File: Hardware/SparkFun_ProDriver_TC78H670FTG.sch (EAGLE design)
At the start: 50 parts, among them J1 POWER_JACKTOE, J2 LATCH, J3 PTH, J4 LATCH, J5 LATCH, J6 PTH, J7 LATCH, J8 PTH, U1 TC78H670FTG, U2 LM1117

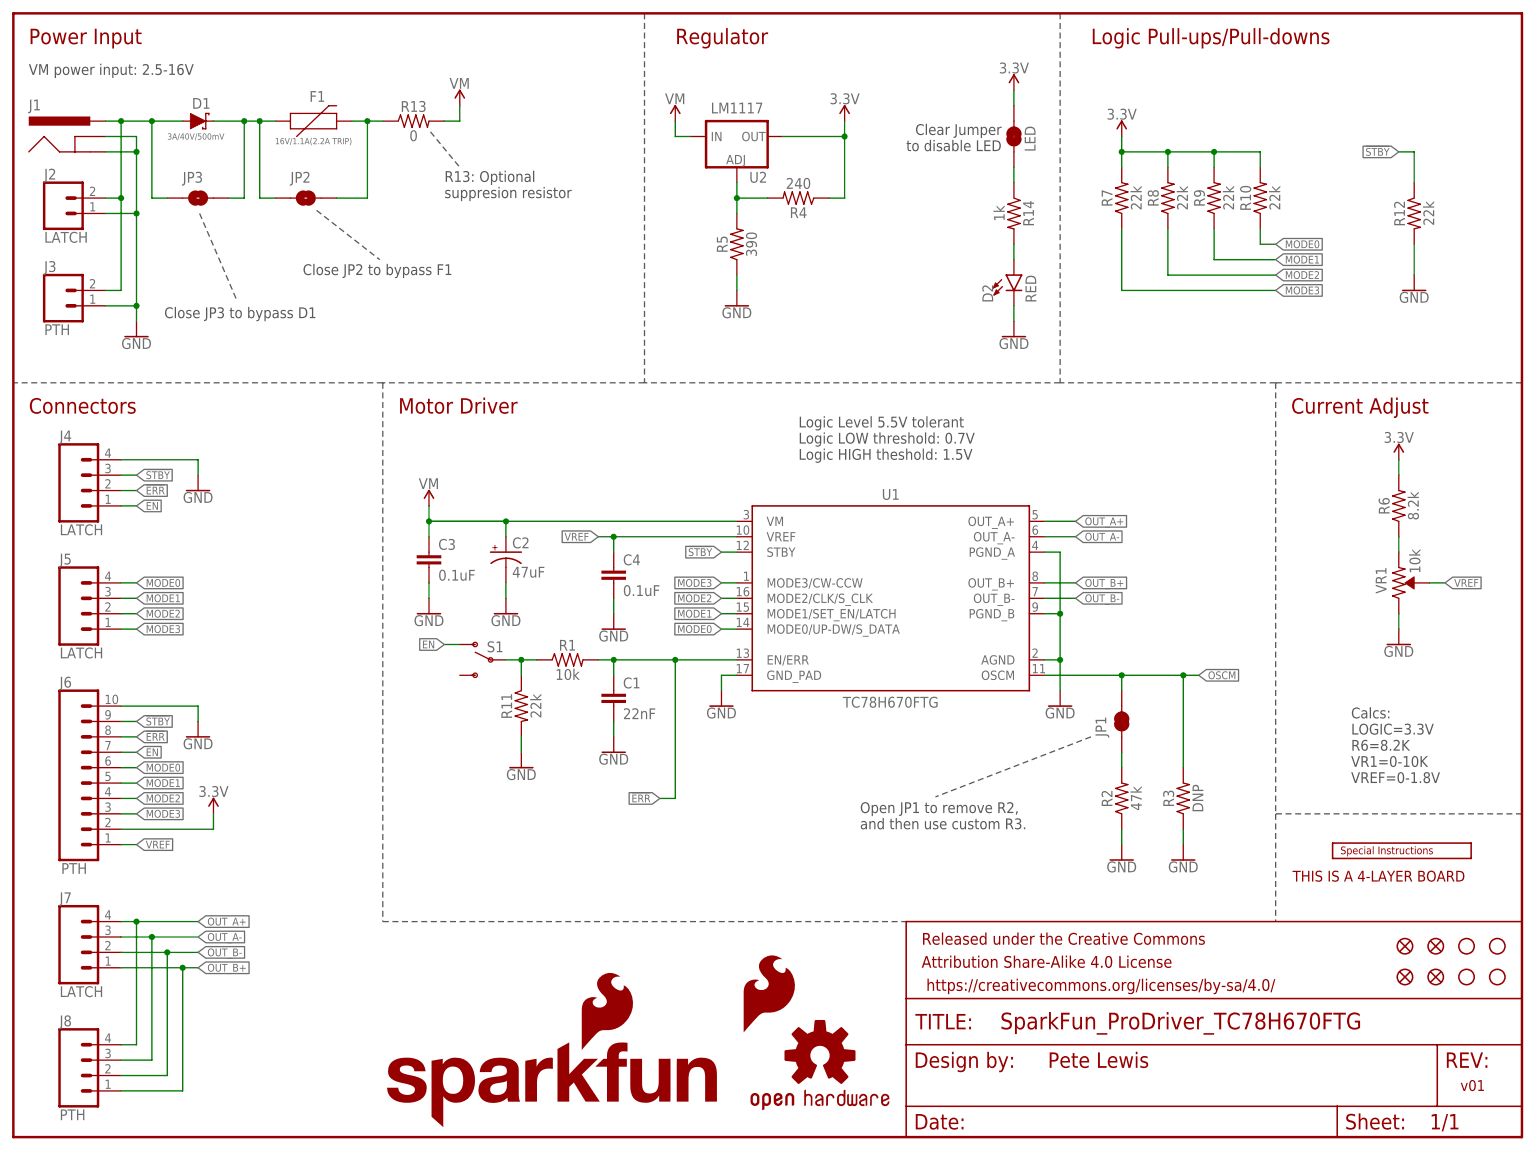
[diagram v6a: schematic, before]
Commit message: Suggestions from design review
-Jumper names same in sch and brd labels
-JP1 to OSCM
-ERR net position aligned with others
-changed power input silk to 3.3V-16V, also updated sch
-added more vias near IC, head sink exposed copper, and VM input traces to help heat transfer to inner layers.
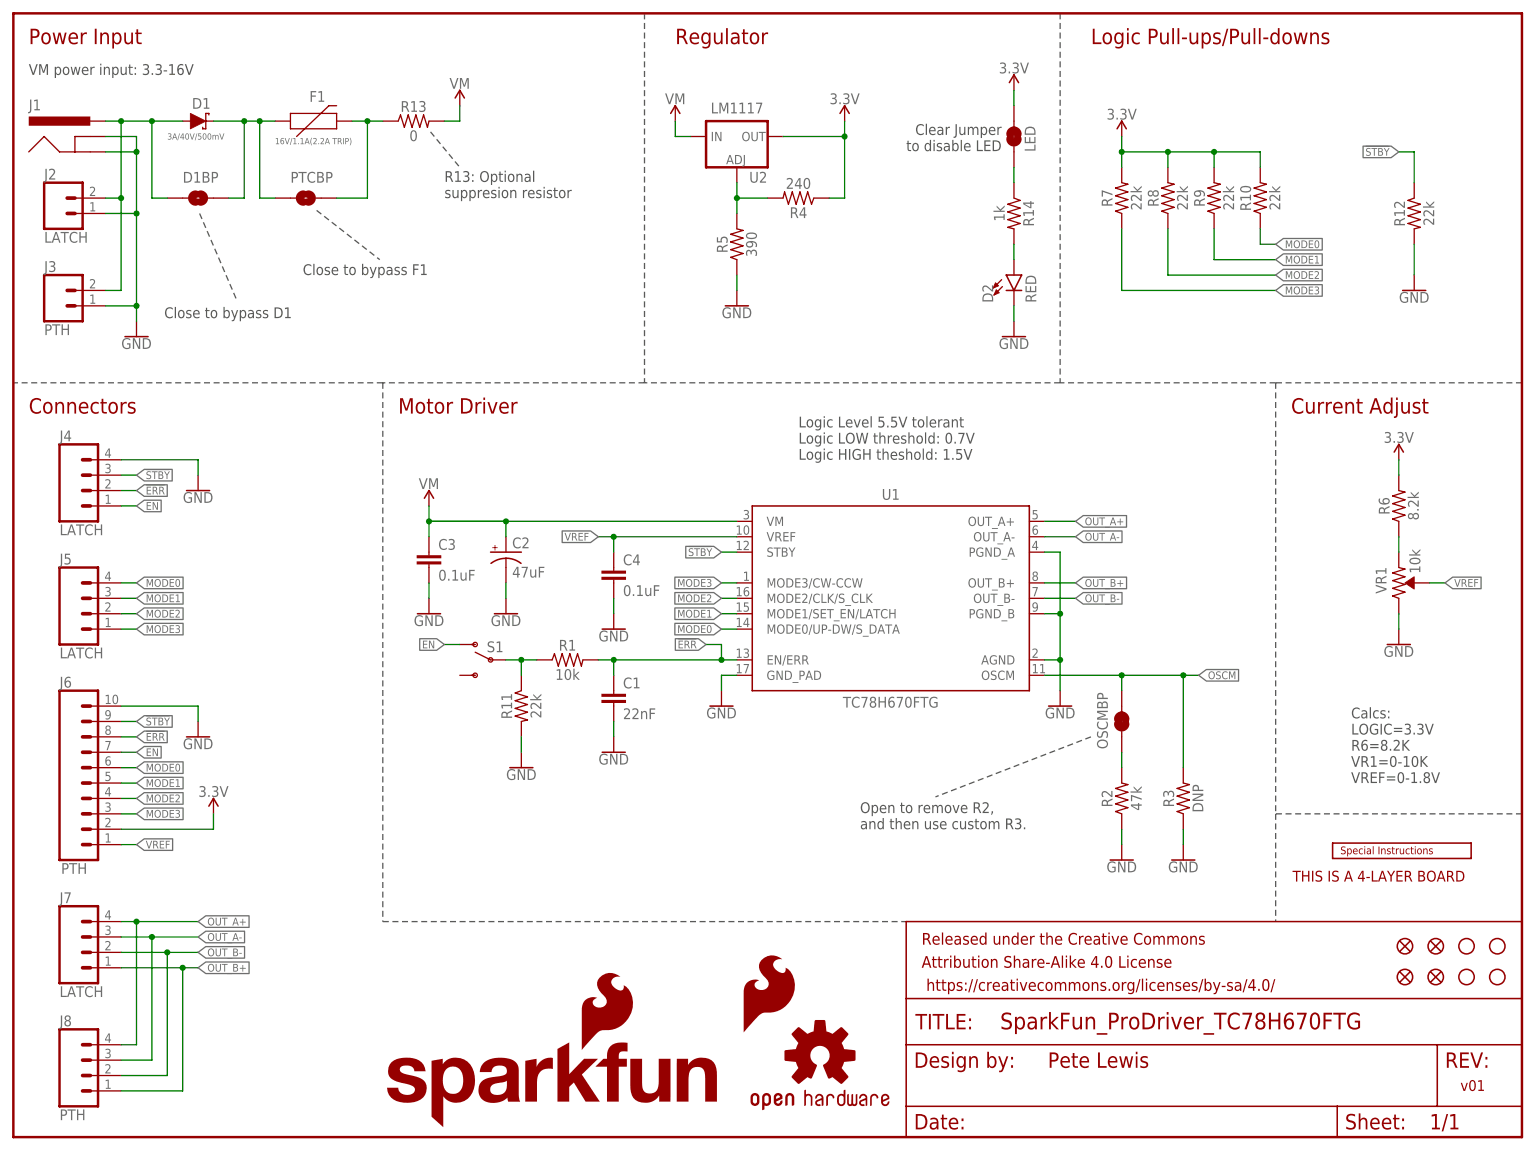
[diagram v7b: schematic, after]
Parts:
- renumbered JP1 to OSCMBP, JP2 to PTCBP, JP3 to D1BP
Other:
- note added: "Close to bypass D1"
- note added: "Close to bypass F1"
- note added: "Open to remove R2, and then use custom R3."
- note added: "VM power input: 3.3-16V"
- note removed: "Close JP2 to bypass F1"
- note removed: "Close JP3 to bypass D1"
- note removed: "Open JP1 to remove R2, and then use custom R3."
- note removed: "VM power input: 2.5-16V"
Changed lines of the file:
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@@
 <part name="R3" library="SparkFun-Resistors" deviceset="RESISTOR" device="AXIAL-0.3" value="DNP"/>
 <part name="GND5" library="SparkFun-PowerSymbols" deviceset="GND" device=""/>
-<part name="JP1" library="SparkFun-Jumpers" deviceset="JUMPER-SMT_2_NC_TRACE" device="_SILK" package3d_urn="urn:adsk.eagle:package:39281/1" value=""/>
+<part name="OSCMBP" library="SparkFun-Jumpers" deviceset="JUMPER-SMT_2_NC_TRACE" device="_SILK" package3d_urn="urn:adsk.eagle:package:39281/1" value=""/>
 <part name="GND6" library="SparkFun-PowerSymbols" deviceset="GND" device=""/>
 <part name="SUPPLY2" library="SparkFun-PowerSymbols" deviceset="VCC" device="" value="VM"/>
@@
 <part name="F1" library="TC78H670FTG" deviceset="PPTC" device="_16V_1.1A_(2.2ATRIP)" value="16V/1.1A(2.2A TRIP)"/>
 <part name="R13" library="SparkFun-Resistors" library_urn="urn:adsk.eagle:library:532" deviceset="0OHM" device="-0603-1/10W-5%" package3d_urn="urn:adsk.eagle:package:39650/1" value="0"/>
-<part name="JP2" library="SparkFun-Jumpers" library_urn="urn:adsk.eagle:library:528" deviceset="JUMPER-SMT_2_NO" device="_SILK" package3d_urn="urn:adsk.eagle:package:39279/1" value=""/>
-<part name="JP3" library="SparkFun-Jumpers" library_urn="urn:adsk.eagle:library:528" deviceset="JUMPER-SMT_2_NO" device="_SILK" package3d_urn="urn:adsk.eagle:package:39279/1" value=""/>
+<part name="PTCBP" library="SparkFun-Jumpers" library_urn="urn:adsk.eagle:library:528" deviceset="JUMPER-SMT_2_NO" device="_SILK" package3d_urn="urn:adsk.eagle:package:39279/1" value=""/>
+<part name="D1BP" library="SparkFun-Jumpers" library_urn="urn:adsk.eagle:library:528" deviceset="JUMPER-SMT_2_NO" device="_SILK" package3d_urn="urn:adsk.eagle:package:39279/1" value=""/>
 <part name="D2" library="SparkFun-LED" deviceset="LED-RED" device="0603" value="RED"/>
 <part name="R14" library="SparkFun-Resistors" deviceset="1KOHM" device="-0603-1/10W-1%" value="1k"/>
@@
 <wire x1="208.28" y1="53.34" x2="208.28" y2="35.56" width="0.2032" layer="97" style="longdash"/>
 <wire x1="104.14" y1="185.42" x2="104.14" y2="124.46" width="0.2032" layer="97" style="longdash"/>
-<text x="139.7" y="50.8" size="1.778" layer="97" font="vector">Open JP1 to remove R2,
+<text x="139.7" y="50.8" size="1.778" layer="97" font="vector">Open to remove R2,
 and then use custom R3.</text>
 <wire x1="177.8" y1="66.04" x2="152.146" y2="56.134" width="0.1524" layer="97" style="shortdash"/>
-<text x="47.752" y="142.24" size="1.778" layer="97" font="vector">Close JP2 to bypass F1</text>
-<text x="24.892" y="135.128" size="1.778" layer="97" font="vector">Close JP3 to bypass D1</text>
+<text x="47.752" y="142.24" size="1.778" layer="97" font="vector">Close to bypass F1</text>
+<text x="24.892" y="135.128" size="1.778" layer="97" font="vector">Close to bypass D1</text>
 <wire x1="30.734" y1="152.4" x2="36.83" y2="138.176" width="0.1524" layer="97" style="shortdash"/>
 <wire x1="50.038" y1="152.908" x2="60.452" y2="144.78" width="0.1524" layer="97" style="shortdash"/>
@@
 to disable LED</text>
 <wire x1="172.72" y1="185.42" x2="172.72" y2="124.46" width="0.2032" layer="97" style="longdash"/>
-<text x="2.54" y="175.26" size="1.778" layer="97" font="vector">VM power input: 2.5-16V</text>
+<text x="2.54" y="175.26" size="1.778" layer="97" font="vector">VM power input: 3.3-16V</text>
 <wire x1="248.92" y1="53.34" x2="208.28" y2="53.34" width="0.2032" layer="97" style="longdash"/>
 <text x="211.074" y="42.164" size="1.778" layer="94" font="vector" ratio="12">THIS IS A 4-LAYER BOARD</text>
@@
 <attribute name="VALUE" x="182.88" y="45.466" size="1.778" layer="96" font="vector" align="top-center"/>
 </instance>
-<instance part="JP1" gate="G$1" x="182.88" y="68.58" smashed="yes" rot="R90">
-<attribute name="NAME" x="180.34" y="66.04" size="1.778" layer="95" font="vector" rot="R90"/>
+<instance part="OSCMBP" gate="G$1" x="182.88" y="68.58" smashed="yes" rot="R90">
+<attribute name="NAME" x="180.594" y="64.008" size="1.778" layer="95" font="vector" rot="R90"/>
 <attribute name="VALUE" x="185.42" y="66.04" size="1.778" layer="96" font="vector" rot="R90" align="top-left"/>
 </instance>
@@
 <attribute name="VALUE" x="66.04" y="166.116" size="1.778" layer="96" font="vector" align="top-center"/>
 </instance>
-<instance part="JP2" gate="G$1" x="48.26" y="154.94" smashed="yes">
+<instance part="PTCBP" gate="G$1" x="48.26" y="154.94" smashed="yes">
 <attribute name="NAME" x="45.72" y="157.48" size="1.778" layer="95" font="vector"/>
 <attribute name="VALUE" x="45.72" y="152.4" size="1.778" layer="96" font="vector" align="top-left"/>
 </instance>
-<instance part="JP3" gate="G$1" x="30.48" y="154.94" smashed="yes">
+<instance part="D1BP" gate="G$1" x="30.48" y="154.94" smashed="yes">
 <attribute name="NAME" x="27.94" y="157.48" size="1.778" layer="95" font="vector"/>
 <attribute name="VALUE" x="27.94" y="152.4" size="1.778" layer="96" font="vector" align="top-left"/>
@@
 <label x="195.58" y="76.2" size="1.27" layer="95" font="vector" xref="yes"/>
 <wire x1="170.18" y1="76.2" x2="182.88" y2="76.2" width="0.1524" layer="91"/>
-<pinref part="JP1" gate="G$1" pin="2"/>
+<pinref part="OSCMBP" gate="G$1" pin="2"/>
 <wire x1="182.88" y1="76.2" x2="193.04" y2="76.2" width="0.1524" layer="91"/>
 <wire x1="193.04" y1="76.2" x2="195.58" y2="76.2" width="0.1524" layer="91"/>
@@
 <pinref part="U1" gate="G$1" pin="EN/ERR"/>
 <pinref part="R1" gate="G$1" pin="2"/>
-<wire x1="119.38" y1="78.74" x2="109.22" y2="78.74" width="0.1524" layer="91"/>
+<wire x1="119.38" y1="78.74" x2="116.84" y2="78.74" width="0.1524" layer="91"/>
 <pinref part="C1" gate="G$1" pin="1"/>
-<wire x1="109.22" y1="78.74" x2="99.06" y2="78.74" width="0.1524" layer="91"/>
+<wire x1="116.84" y1="78.74" x2="99.06" y2="78.74" width="0.1524" layer="91"/>
 <wire x1="99.06" y1="78.74" x2="96.52" y2="78.74" width="0.1524" layer="91"/>
 <wire x1="99.06" y1="76.2" x2="99.06" y2="78.74" width="0.1524" layer="91"/>
 <junction x="99.06" y="78.74"/>
-<wire x1="109.22" y1="78.74" x2="109.22" y2="55.88" width="0.1524" layer="91"/>
-<junction x="109.22" y="78.74"/>
-<wire x1="109.22" y1="55.88" x2="106.68" y2="55.88" width="0.1524" layer="91"/>
-<label x="106.68" y="55.88" size="1.27" layer="95" font="vector" rot="R180" xref="yes"/>
+<wire x1="116.84" y1="78.74" x2="116.84" y2="81.28" width="0.1524" layer="91"/>
+<junction x="116.84" y="78.74"/>
+<wire x1="116.84" y1="81.28" x2="114.3" y2="81.28" width="0.1524" layer="91"/>
+<label x="114.3" y="81.28" size="1.27" layer="95" font="vector" rot="R180" xref="yes"/>
 </segment>
 <segment>
@@
 <segment>
 <pinref part="R2" gate="G$1" pin="2"/>
-<pinref part="JP1" gate="G$1" pin="1"/>
+<pinref part="OSCMBP" gate="G$1" pin="1"/>
 <wire x1="182.88" y1="60.96" x2="182.88" y2="63.5" width="0.1524" layer="91"/>
 </segment>
@@
 <wire x1="17.78" y1="167.64" x2="22.86" y2="167.64" width="0.1524" layer="91"/>
 <junction x="17.78" y="167.64"/>
-<pinref part="JP3" gate="G$1" pin="1"/>
+<pinref part="D1BP" gate="G$1" pin="1"/>
 <wire x1="22.86" y1="167.64" x2="27.94" y2="167.64" width="0.1524" layer="91"/>
 <wire x1="25.4" y1="154.94" x2="22.86" y2="154.94" width="0.1524" layer="91"/>
@@
 <pinref part="F1" gate="F1" pin="1"/>
 <wire x1="33.02" y1="167.64" x2="38.1" y2="167.64" width="0.1524" layer="91"/>
-<pinref part="JP3" gate="G$1" pin="2"/>
+<pinref part="D1BP" gate="G$1" pin="2"/>
 <wire x1="38.1" y1="167.64" x2="40.64" y2="167.64" width="0.1524" layer="91"/>
 <wire x1="40.64" y1="167.64" x2="43.18" y2="167.64" width="0.1524" layer="91"/>
@@
 <junction x="40.64" y="167.64"/>
 <wire x1="40.64" y1="154.94" x2="43.18" y2="154.94" width="0.1524" layer="91"/>
-<pinref part="JP2" gate="G$1" pin="1"/>
+<pinref part="PTCBP" gate="G$1" pin="1"/>
 </segment>
 </net>
@@
 <wire x1="55.88" y1="167.64" x2="58.42" y2="167.64" width="0.1524" layer="91"/>
 <wire x1="58.42" y1="167.64" x2="58.42" y2="154.94" width="0.1524" layer="91"/>
-<pinref part="JP2" gate="G$1" pin="2"/>
+<pinref part="PTCBP" gate="G$1" pin="2"/>
 <wire x1="58.42" y1="154.94" x2="53.34" y2="154.94" width="0.1524" layer="91"/>
 <pinref part="R13" gate="G$1" pin="1"/>

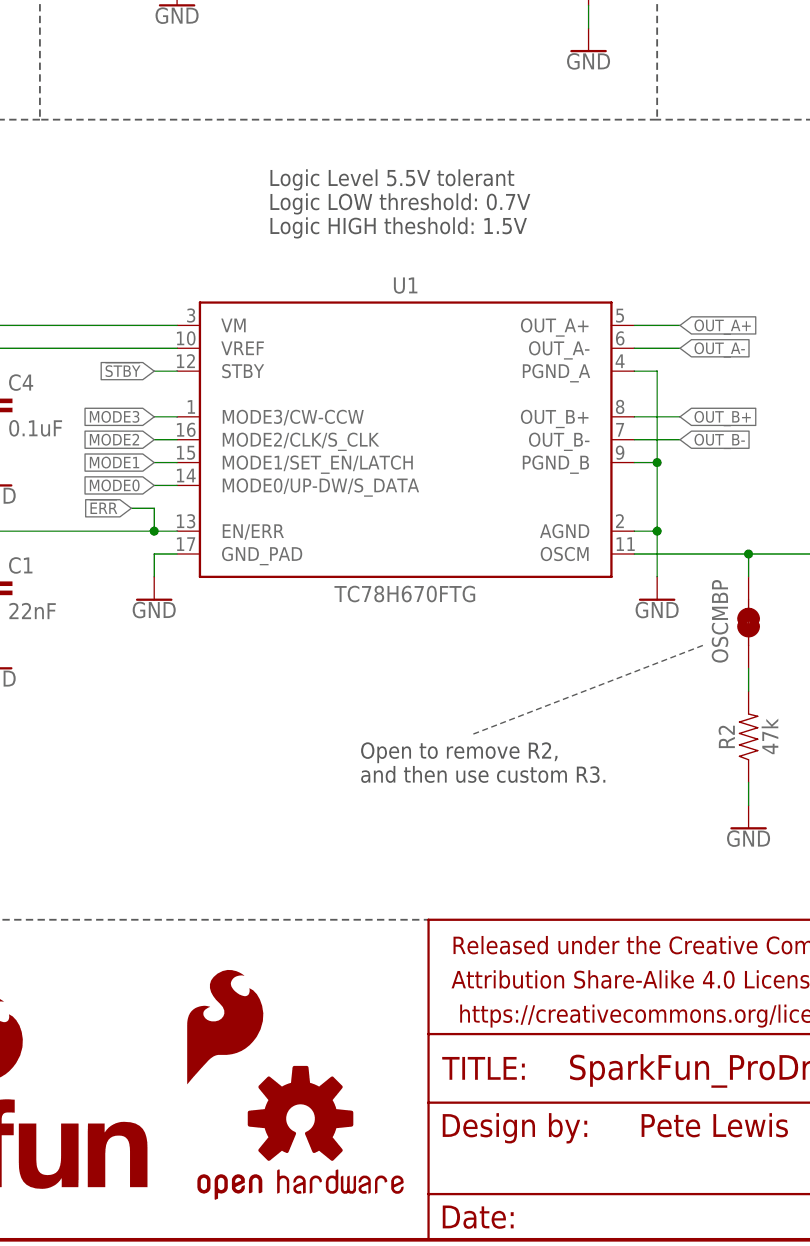
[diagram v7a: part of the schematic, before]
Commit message: Double-check fixes
-Eagle Library had storefront SKUs for latch terminals. Corrected to prod IDs.
-removed unnecessary flame symbol in sch (lcopied a second footprint to keep in board).
-text font to vector on one sch paragraph
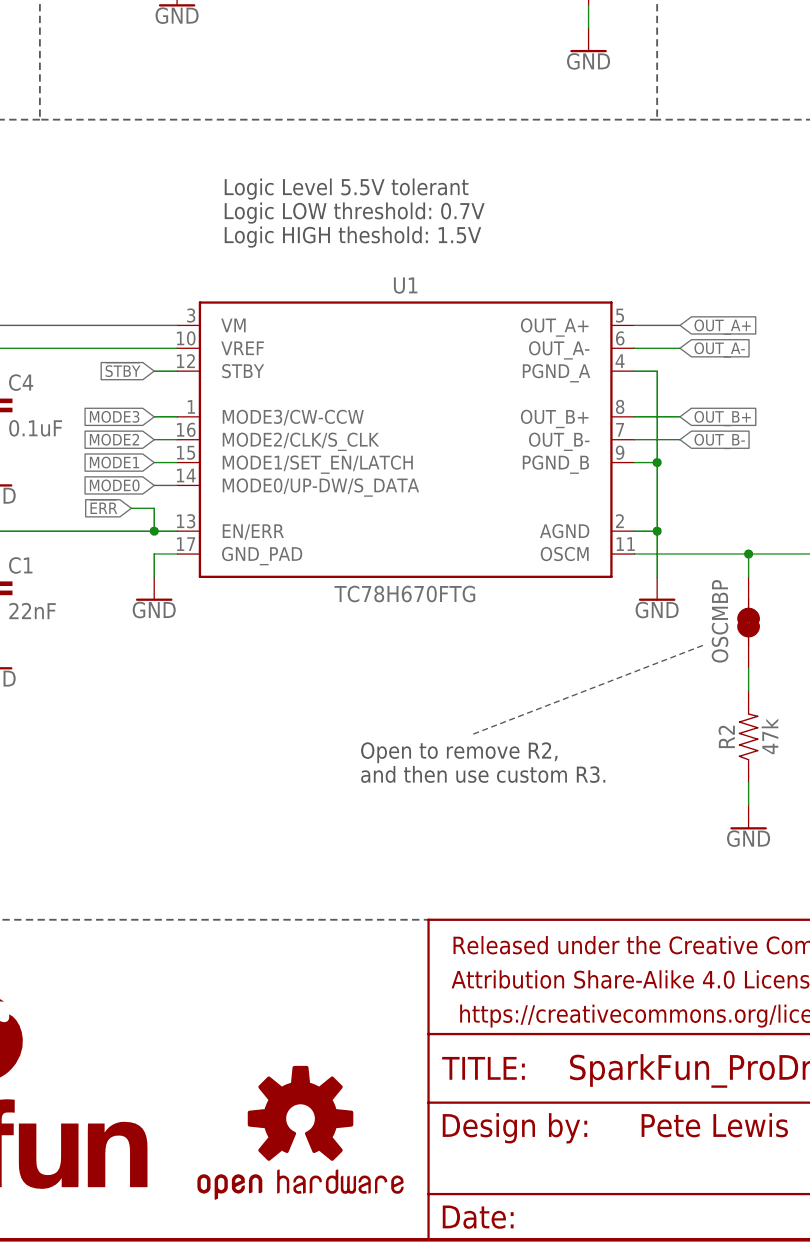
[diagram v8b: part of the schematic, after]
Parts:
- removed LOGO4: SFE_LOGO_FLAME.1_INCH, SparkFun-Aesthetics:SFE_LOGO_FLAME.1_INCH
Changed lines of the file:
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@@
 <part name="LOGO2" library="SparkFun-Aesthetics" deviceset="OSHW-LOGO" device="S"/>
 <part name="FRAME1" library="SparkFun-Aesthetics" deviceset="FRAME-LETTER" device=""/>
-<part name="LOGO4" library="SparkFun-Aesthetics" deviceset="SFE_LOGO_FLAME" device=".1_INCH" value="SFE_LOGO_FLAME.1_INCH"/>
 <part name="FID3" library="SparkFun-Aesthetics" deviceset="FIDUCIAL" device="1X2" value="FIDUCIAL1X2"/>
 <part name="FID4" library="SparkFun-Aesthetics" deviceset="FIDUCIAL" device="1X2" value="FIDUCIAL1X2"/>
@@
 <wire x1="248.92" y1="53.34" x2="208.28" y2="53.34" width="0.2032" layer="97" style="longdash"/>
 <text x="211.074" y="42.164" size="1.778" layer="94" font="vector" ratio="12">THIS IS A 4-LAYER BOARD</text>
-<text x="129.54" y="111.76" size="1.778" layer="97">Logic Level 5.5V tolerant
+<text x="124.46" y="110.744" size="1.778" layer="97" font="vector">Logic Level 5.5V tolerant
 Logic LOW threshold: 0.7V
 Logic HIGH theshold: 1.5V</text>
@@
 <attribute name="DRAWING_NAME" x="162.814" y="17.78" size="2.7432" layer="94" font="vector"/>
 </instance>
-<instance part="LOGO4" gate="G$1" x="120.142" y="16.764" smashed="yes"/>
 <instance part="FID3" gate="G$1" x="229.616" y="26.416" smashed="yes"/>
 <instance part="FID4" gate="G$1" x="229.616" y="31.496" smashed="yes"/>
